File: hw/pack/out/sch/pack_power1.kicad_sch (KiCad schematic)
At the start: 20 parts, among them Q1 DMG2305UX, SW1 recessed slide, U4 TPS61023, U5 TLV75533P, U6 TLV75533P

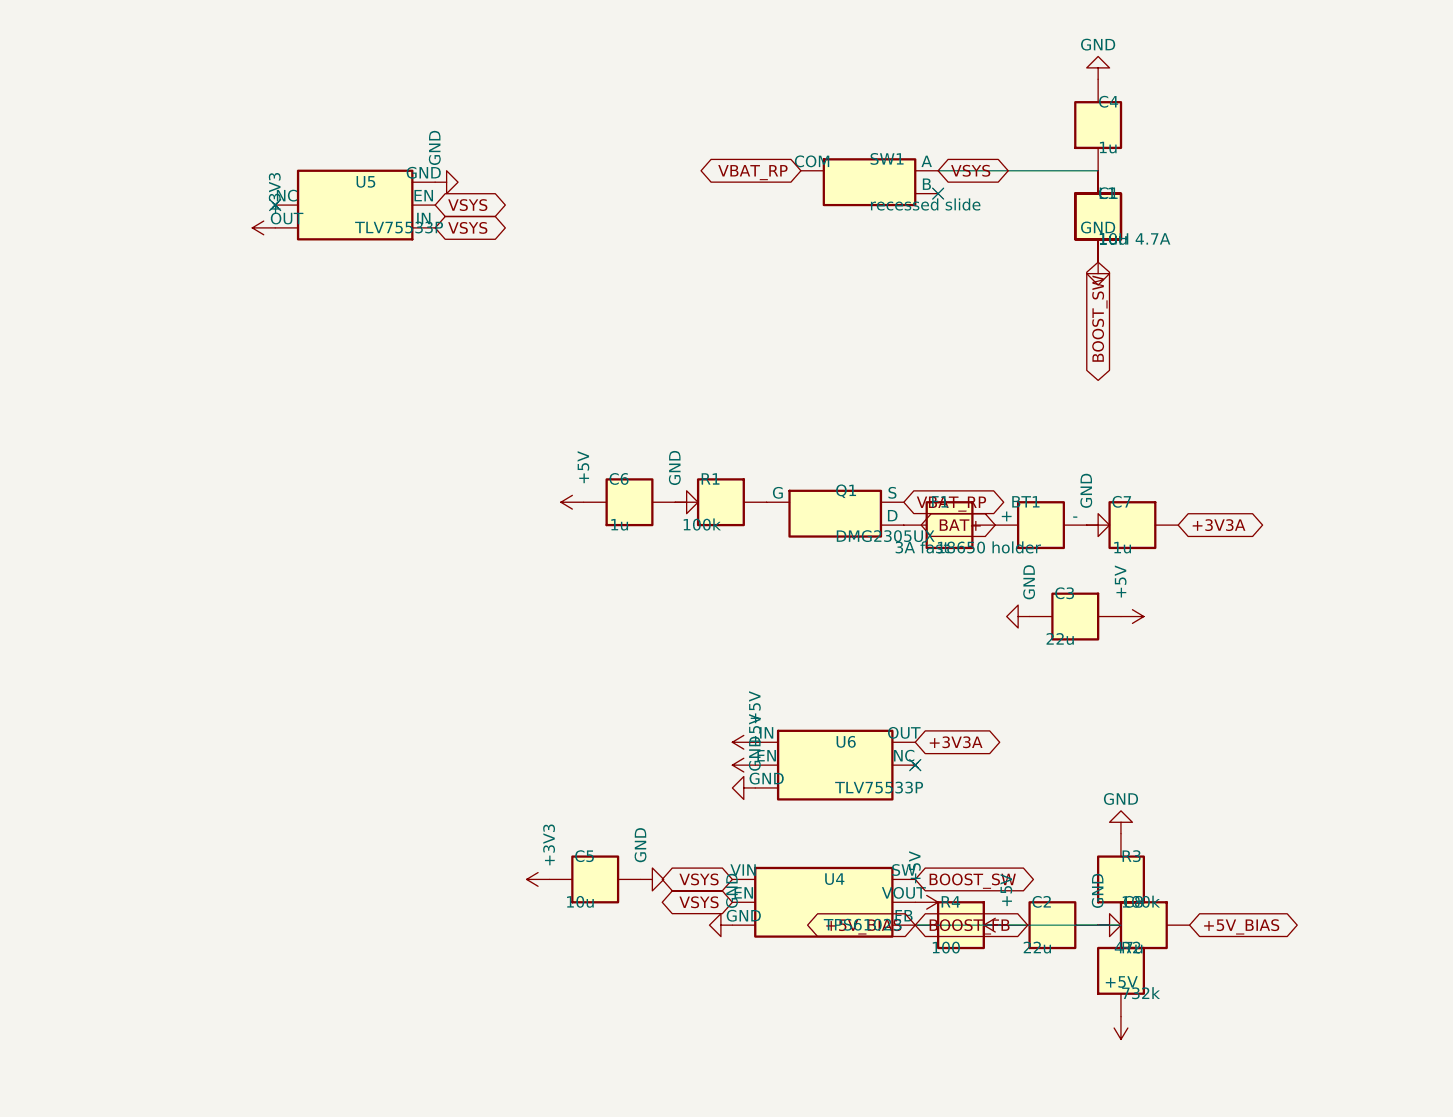
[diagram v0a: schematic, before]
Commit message: pack: cost-down to PK-12 $33.34: printed cell cradle + MYOUNG contacts, LCSC IPEX pigtail, priced M2 screws (#34)
- BT1: MYOUNG MY-18650-04-J/-05-J (LCSC C19184125/C19184124) in a printed
  cradle in the base (76 mm plate faces: spring 4.2-9.2 mm for 70-65 mm cells);
  the SMT BH-18650-B1BA002 holder is gone; footprint Cell_Wire_Pads
- pigtail: BAT Wireless BWIPX1-SMA-1.13L150 (LCSC C784404, $0.6015 @100), SMA
  cut off, ~100 mm + 31 mm wire whip; audit.py PIGTAIL_IL 0.46 <= 0.6 dB
- audit.py cutoff path includes the spring (0.10 ohm), cutoff stays 3.2 V
- 2 x M2x6 PT screws $0.112 (Fastener Superstore 585907)
- prices.py, bom.csv, pack_uk.csv (UK $34.81) updated

Co-Authored-By: Claude Opus 5.5 <noreply@anthropic.com>
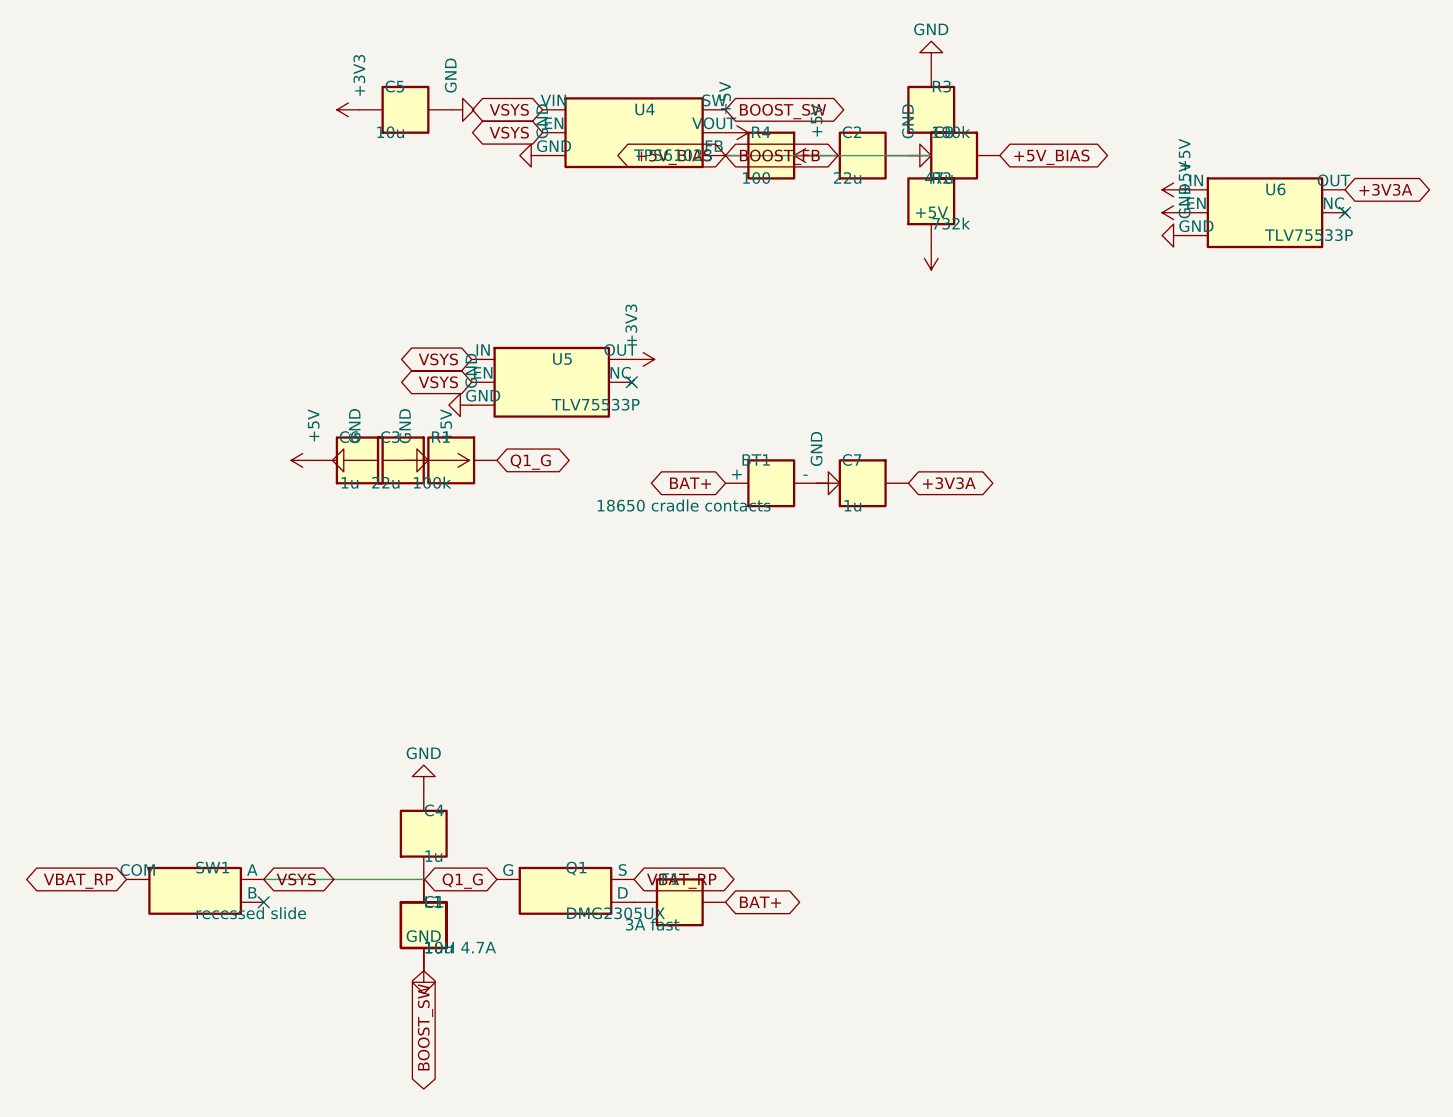
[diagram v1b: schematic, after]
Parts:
- BT1: value 18650 holder -> 18650 cradle contacts; footprint openpack:BH-18650-B1BA002 -> openpack:Cell_Wire_Pads; MPN BH-18650-B1BA002 -> MY-18650-04-J/05-J
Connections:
- net Q1_G: now reaches Q1.1 (G), R1.1
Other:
- moved on the sheet: BT1, C1, C2, C3, C4, C5, C6, C7, C8, F1, L1, Q1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

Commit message: pack: #104 review fixes: 1 mm L1 battery path, test points, clip inserts off the antenna, pigtail route, JLC LCSC/rotations (#34)
- router: 'bat' class (1.0 mm, L1 only, necks <=1.36 mm at small pads);
  SW1 on-throw moved to pin 3 so feed and VSYS don't cross; 40 mOhm path
- audit.py: cell path from the board tracks (121 mOhm total, est. spring):
  cutoff computes 3.2012 V -> rounds to 3.3 V (reported, not tuned)
- TP3-TP11 folded in from review-104-tps (415194b), TP5/TP9-11 moved
- mech: clip inserts to (-24,3)/(-24,17) under the board; PIGTAIL route,
  bend radius, tie-down; fit.py checks both
- outputs: LCSC # per BOM line (verified), DNP/CONSIGN, CPL rotation table
- tests: battery path layer/width/R, BOM LCSC-or-DNP, rotation table

Co-Authored-By: Claude Opus 5.5 <noreply@anthropic.com>
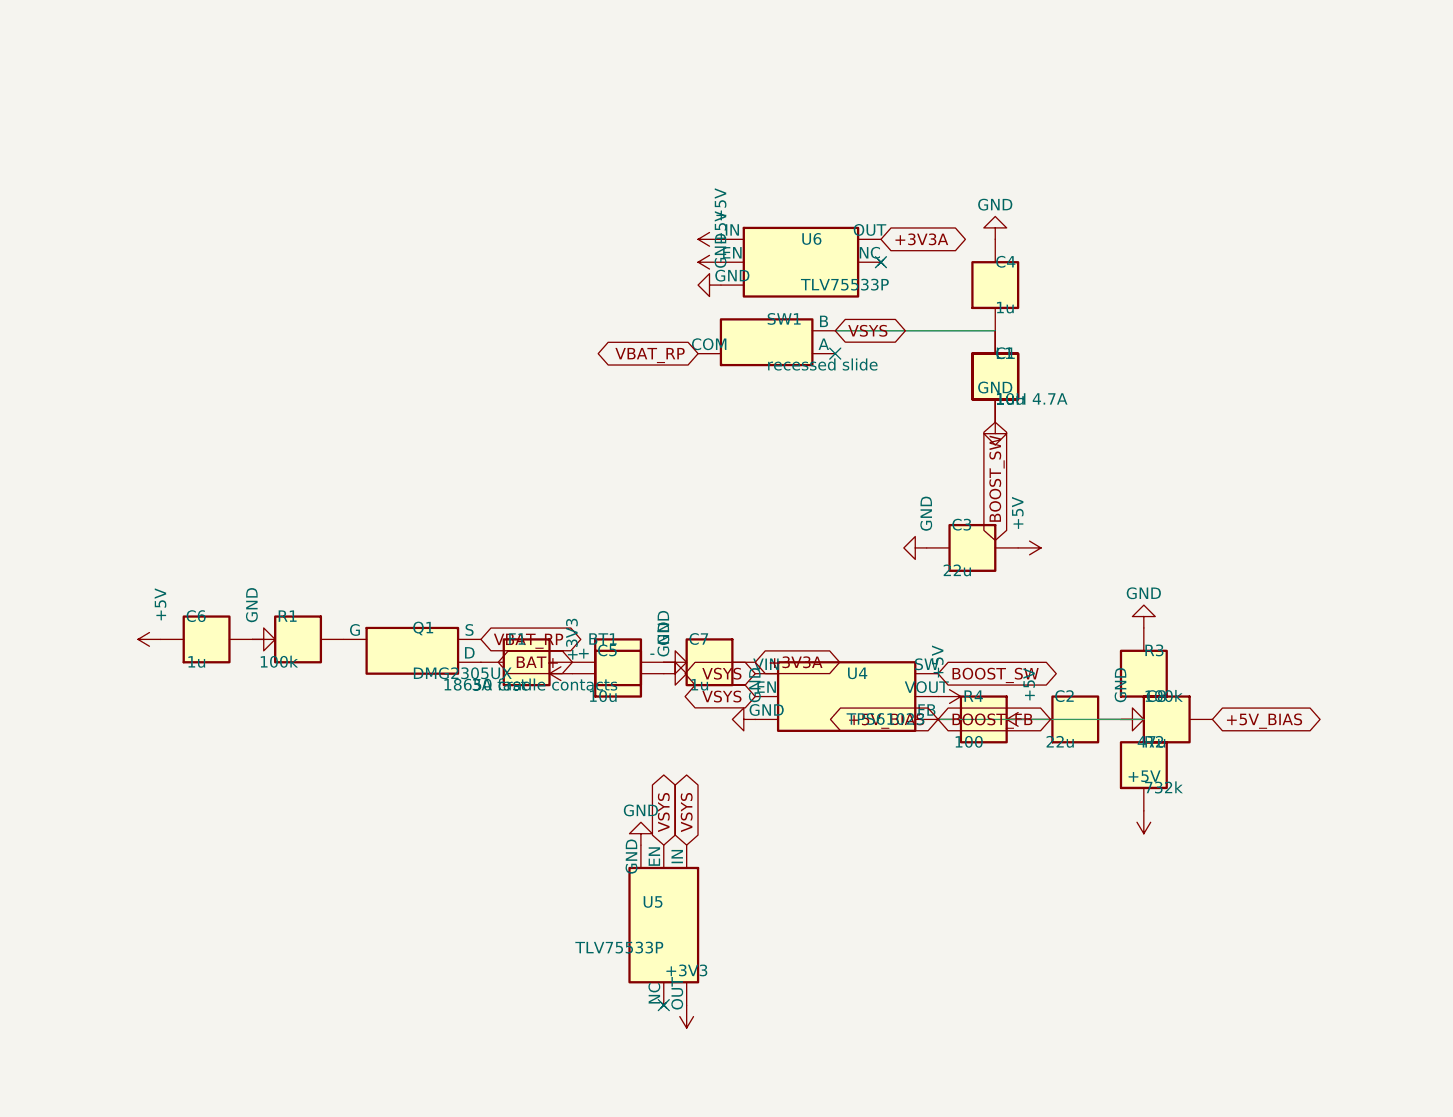
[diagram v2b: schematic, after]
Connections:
- net VSYS: now also SW1.3 (B); no longer SW1.1 (A)
- net Q1_G: no longer names the net of Q1.1 (G), R1.1
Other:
- moved on the sheet: BT1, C1, C2, C3, C4, C5, C6, C7, C8, F1, L1, Q1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
